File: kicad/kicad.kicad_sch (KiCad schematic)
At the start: 28 parts, among them J1 OLED_128x64, SW1 RotaryEncoder_Switch, SW2 SW_Wuerth_450301014042

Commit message: updated schematic and pcb
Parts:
- removed LED1: LED_5mm, PCM_LED_THT_AKL:LED_D5.0mm, symbol PCM_LED_AKL:LED_5mm
- added A1: Adafruit_Feather_V2, Module:Adafruit_Feather, symbol MCU_Module:Adafruit_Feather_Generic
- S1, S10, S11, S12, S2, S3, S4, S5, S6, S7, S8, S9: footprint (none) -> PCM_Switch_Keyboard_Hotswap_Kailh:SW_Hotswap_Kailh_MX_1.00u
- SW1: footprint (none) -> ScottoKeebs_Scotto:Encoder_EC11_MX
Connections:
- net +3V3: now also A1.2 (3V); no longer J1.2 (VCC)
- net COL0: now also A1.20 (13)
- net COL1: now also A1.21 (12)
- net COL2: now also A1.22 (27)
- net ENC_CLK: now also A1.5 (A0)
- net ENC_DT: now also A1.6 (A1)
- net ENC_SW: now also A1.7 (A2)
- net GND: now also SW2.2 (C), A1.4 (GND); no longer J1.1 (GND)
- net ROW0: now also A1.23 (33)
- net ROW1: now also A1.24 (15)
- net ROW2: now also A1.25 (32)
- net ROW3: now also A1.26 (14)
- net BT_SELECT: now reaches SW2.1 (B)
- net BT_SELECT: now also A1.8 (A3)
- net I2C_SCL: no longer names the net of J1.3 (SCL)
- net I2C_SDA: no longer names the net of J1.4 (SDA)
- no-connect marks 0 -> 5
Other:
- note added: "Connected with STEMMA QT directly to the board"

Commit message: modified layout to be 3 row 4 col instead of 3 col 4 row. added mounting holes
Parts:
- added H1, H2, H3, H4: MountingHole, MountingHole:MountingHole_2.2mm_M2, symbol Mechanical:MountingHole
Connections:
- net ROW3 is gone; now on net ROW2: A1.26 (14), D10.1 (K), D11.1 (K), D12.1 (K)
- net BT_SELECT: now also A1.6 (A1); no longer A1.8 (A3)
- net COL0: now also S5.1, S9.1; no longer S10.1, S4.1, S7.1
- net COL1: now also S10.1, S6.1; no longer S11.1, S5.1, S8.1
- net COL2: now also S11.1, S7.1; no longer S12.1, S6.1, S9.1
- net ENC_CLK: now also A1.8 (A3); no longer A1.5 (A0)
- net ENC_DT: now also A1.5 (A0); no longer A1.6 (A1)
- net ENC_SW: now also SW1.S2; no longer SW1.S1
- net GND: now also SW1.S1; no longer SW1.S2
- net ROW0: now also A1.24 (15), D4.1 (K); no longer A1.23 (33)
- net ROW1: now also A1.25 (32), D7.1 (K), D8.1 (K); no longer A1.24 (15), D4.1 (K)
- net ROW2: no longer A1.25 (32), D7.1 (K), D8.1 (K)
- new net COL3: A1.23 (33), S12.1, S4.1, S8.1
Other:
- moved on the sheet: A1, J1, SW1, SW2

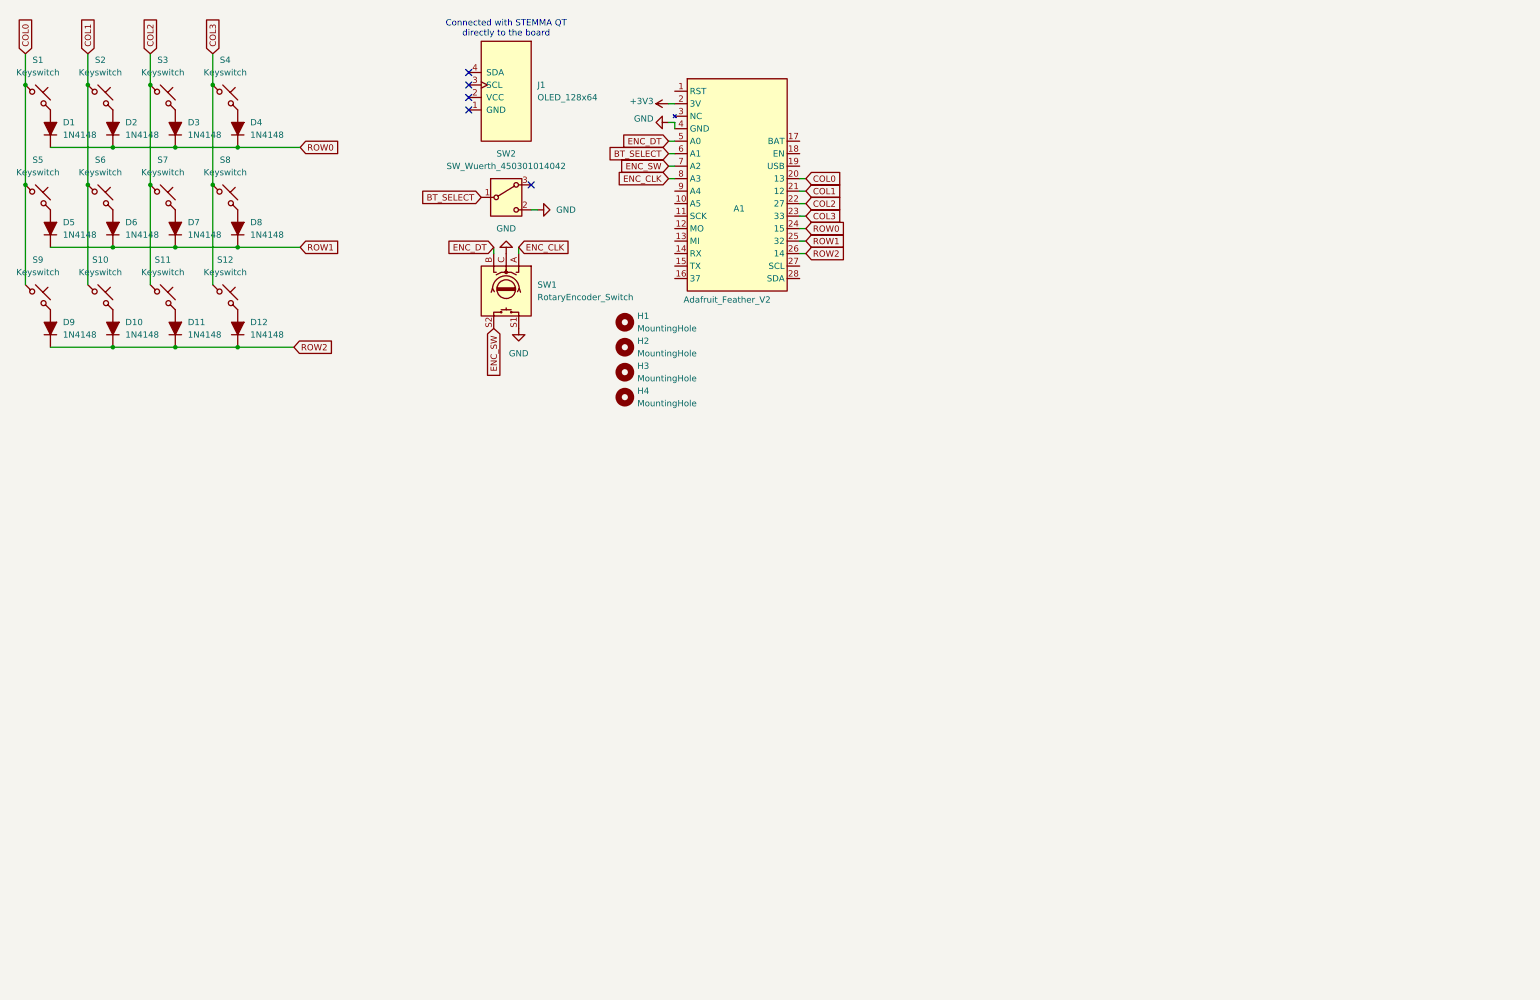
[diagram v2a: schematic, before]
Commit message: Updated schematic to change from single pcb to sandwich pcb.
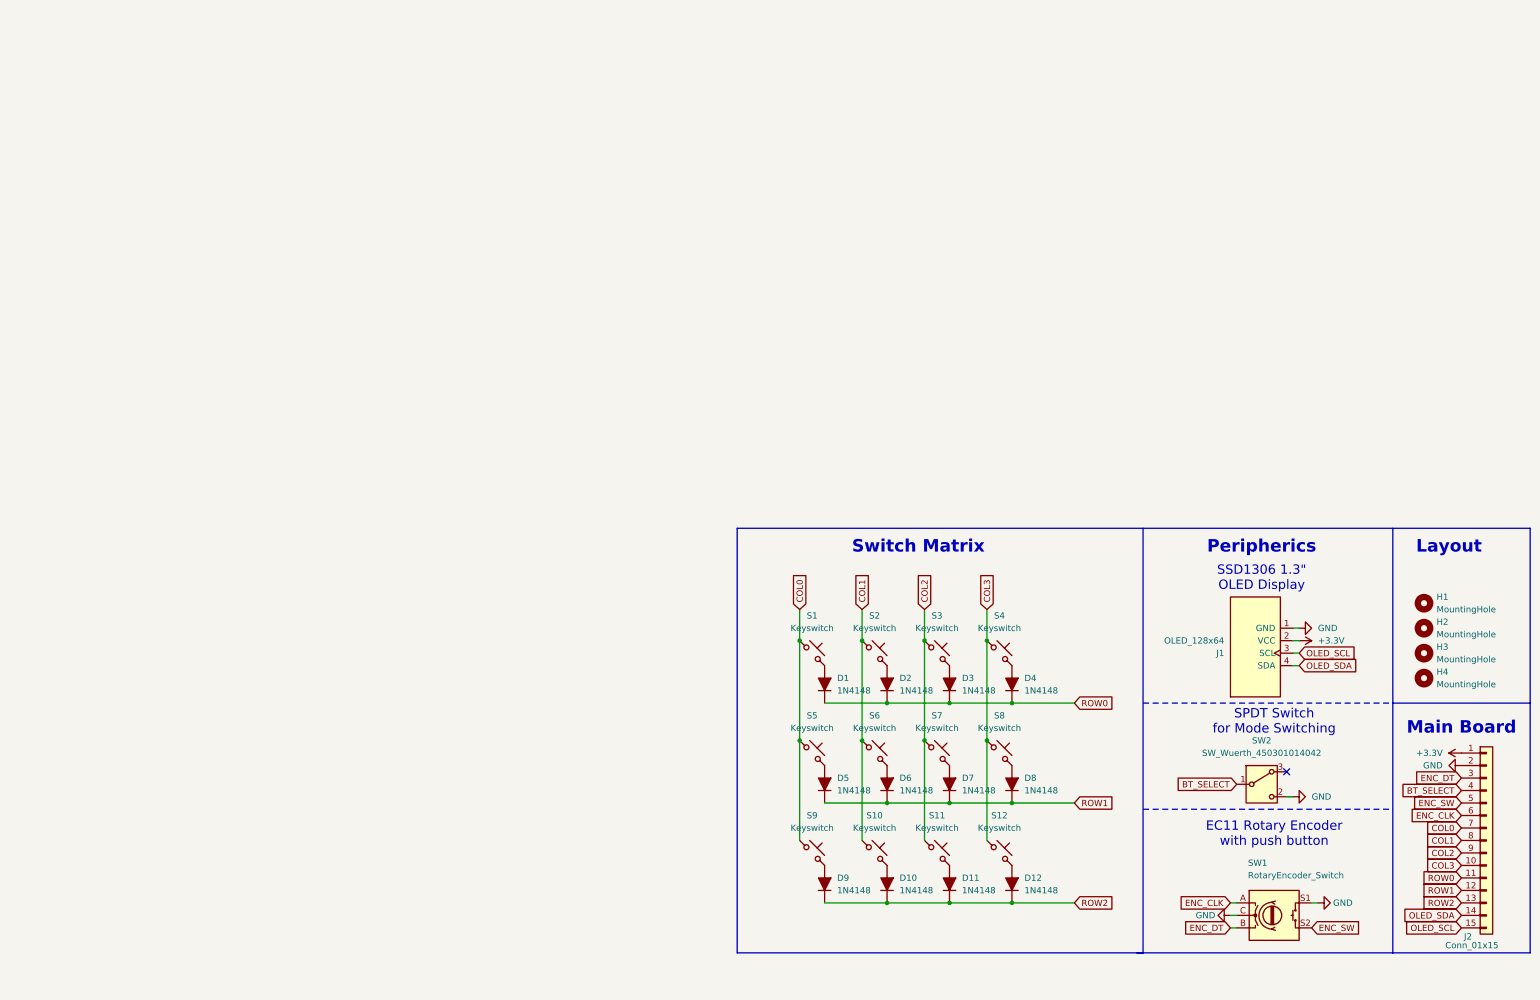
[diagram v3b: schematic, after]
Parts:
- removed A1: Adafruit_Feather_V2, Module:Adafruit_Feather, symbol MCU_Module:Adafruit_Feather_Generic
- added J2: Conn_01x15, symbol Connector_Generic:Conn_01x15
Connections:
- net BT_SELECT: now also J2.4 (Pin_4)
- net COL0: now also J2.7 (Pin_7)
- net COL1: now also J2.8 (Pin_8)
- net COL2: now also J2.9 (Pin_9)
- net COL3: now also J2.10 (Pin_10)
- net ENC_CLK: now also J2.6 (Pin_6)
- net ENC_DT: now also J2.3 (Pin_3)
- net ENC_SW: now also J2.5 (Pin_5)
- net GND: now also J1.1 (GND), J2.2 (Pin_2)
- net ROW0: now also J2.11 (Pin_11)
- net ROW1: now also J2.12 (Pin_12)
- net ROW2: now also J2.13 (Pin_13)
- net +3.3V: now reaches J1.2 (VCC)
- net +3.3V: now also J2.1 (Pin_1)
- net OLED_SCL: now reaches J1.3 (SCL)
- net OLED_SCL: now also J2.15 (Pin_15)
- net OLED_SDA: now reaches J1.4 (SDA)
- net OLED_SDA: now also J2.14 (Pin_14)
- no-connect marks 5 -> 1
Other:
- note added: "EC11 Rotary Encoder with push button"
- note added: "Layout"
- note added: "Main Board"
- note added: "Peripherics"
- note added: "SPDT Switch for Mode Switching"
- note added: "SSD1306 1.3" OLED Display"
- note added: "Switch Matrix"
- note removed: "Connected with STEMMA QT directly to the board"
- moved on the sheet: D1, D10, D11, D12, D2, D3, D4, D5, D6, D7, D8, D9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

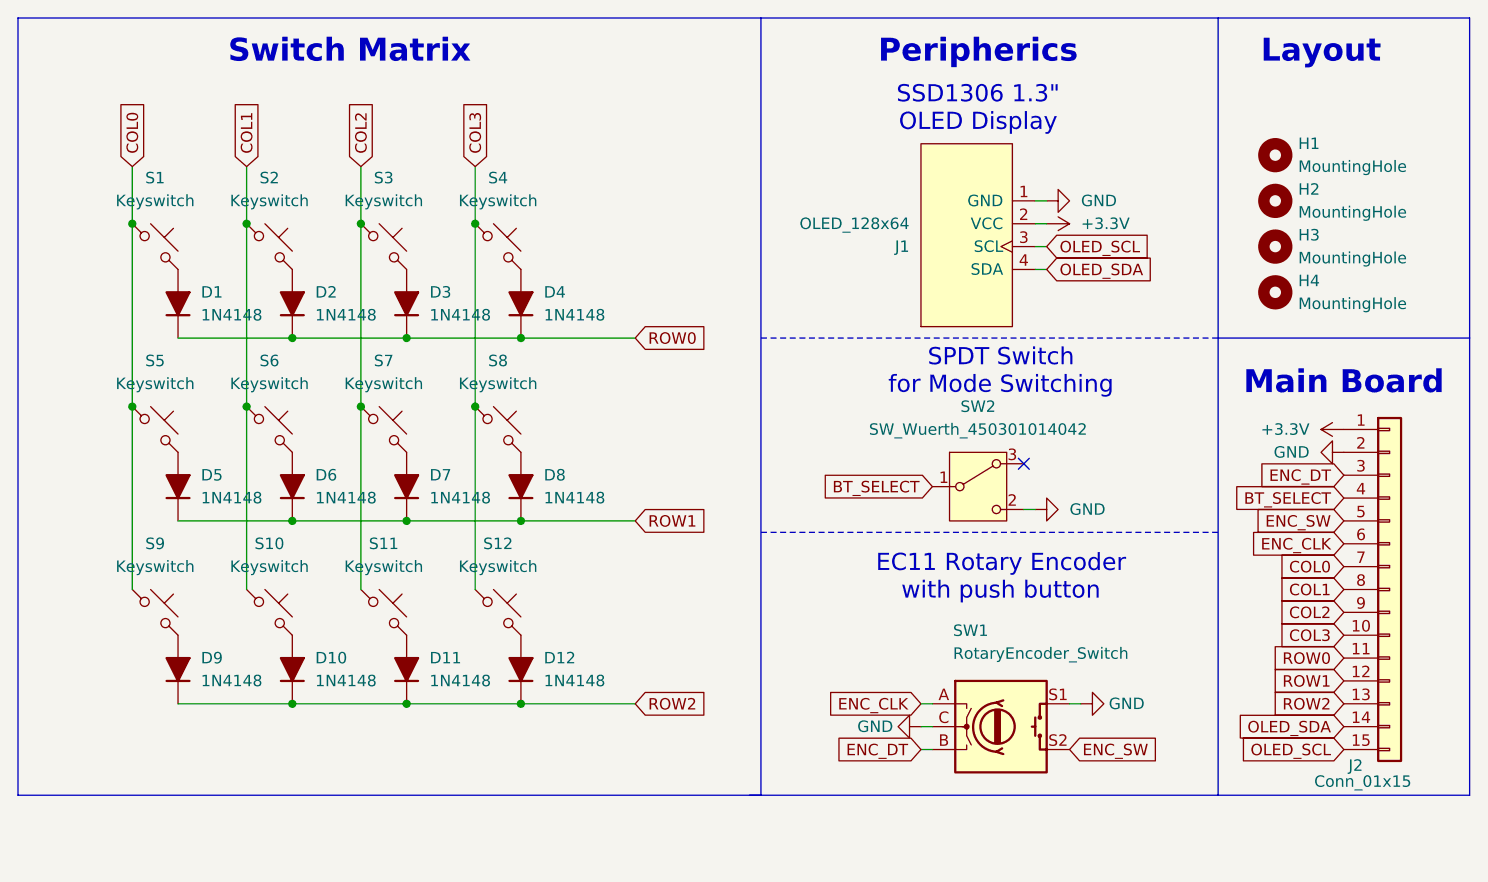
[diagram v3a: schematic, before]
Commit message: added 3d model for oled 128 x 64. went back to 3 x 4 format
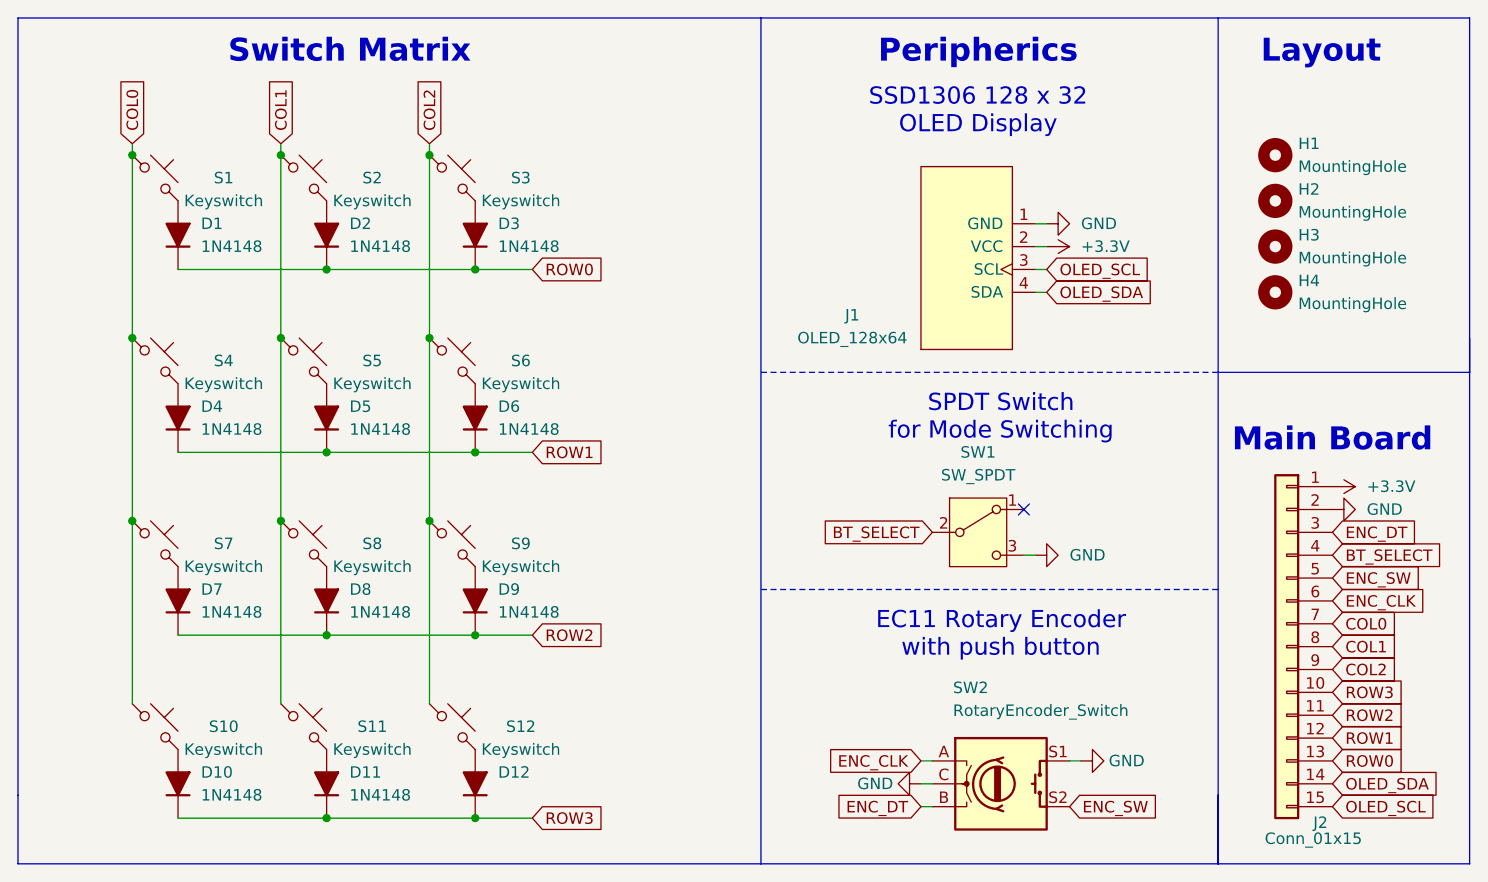
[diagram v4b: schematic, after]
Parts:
- removed D4, D8: 1N4148, PCM_Diode_THT_AKL:D_DO-35_SOD27_P7.62mm_Horizontal, symbol PCM_Diode_AKL:1N4148
- removed S4, S8: Keyswitch, PCM_Switch_Keyboard_Hotswap_Kailh:SW_Hotswap_Kailh_MX_1.00u, symbol ScottoKeebs:Placeholder_Keyswitch
- removed SW2: SW_Wuerth_450301014042, Button_Switch_THT:SW_Slide-03_Wuerth-WS-SLTV_10x2.5x6.4_P2.54mm, symbol Switch:SW_Wuerth_450301014042
- added D10, D11: 1N4148, Diode_THT:D_DO-35_SOD27_P7.62mm_Horizontal, symbol PCM_Diode_AKL:1N4148
- added S10, S11: Keyswitch, ScottoKeebs_Scotto:MX_Hotswap_1.00u, symbol ScottoKeebs:Placeholder_Keyswitch
- added SW1: SW_SPDT, Button_Switch_THT:SW_Slide_SPDT_Angled_CK_OS102011MA1Q, symbol Switch:SW_SPDT
- D1, D12, D2, D3: footprint PCM_Diode_THT_AKL:D_DO-35_SOD27_P7.62mm_Horizontal -> Diode_THT:D_DO-35_SOD27_P7.62mm_Horizontal
- D4: renamed from D5; footprint PCM_Diode_THT_AKL:D_DO-35_SOD27_P7.62mm_Horizontal -> Diode_THT:D_DO-35_SOD27_P7.62mm_Horizontal
- D5: renamed from D6; footprint PCM_Diode_THT_AKL:D_DO-35_SOD27_P7.62mm_Horizontal -> Diode_THT:D_DO-35_SOD27_P7.62mm_Horizontal
- D6: renamed from D7; footprint PCM_Diode_THT_AKL:D_DO-35_SOD27_P7.62mm_Horizontal -> Diode_THT:D_DO-35_SOD27_P7.62mm_Horizontal
- D7: renamed from D9; footprint PCM_Diode_THT_AKL:D_DO-35_SOD27_P7.62mm_Horizontal -> Diode_THT:D_DO-35_SOD27_P7.62mm_Horizontal
- D8: renamed from D10; footprint PCM_Diode_THT_AKL:D_DO-35_SOD27_P7.62mm_Horizontal -> Diode_THT:D_DO-35_SOD27_P7.62mm_Horizontal
- D9: renamed from D11; footprint PCM_Diode_THT_AKL:D_DO-35_SOD27_P7.62mm_Horizontal -> Diode_THT:D_DO-35_SOD27_P7.62mm_Horizontal
- J2: footprint (none) -> Connector_PinHeader_2.54mm:PinHeader_1x15_P2.54mm_Vertical
- S1, S12, S2, S3: footprint PCM_Switch_Keyboard_Hotswap_Kailh:SW_Hotswap_Kailh_MX_1.00u -> ScottoKeebs_Scotto:MX_Hotswap_1.00u
- S4: renamed from S5; footprint PCM_Switch_Keyboard_Hotswap_Kailh:SW_Hotswap_Kailh_MX_1.00u -> ScottoKeebs_Scotto:MX_Hotswap_1.00u
- S5: renamed from S6; footprint PCM_Switch_Keyboard_Hotswap_Kailh:SW_Hotswap_Kailh_MX_1.00u -> ScottoKeebs_Scotto:MX_Hotswap_1.00u
- S6: renamed from S7; footprint PCM_Switch_Keyboard_Hotswap_Kailh:SW_Hotswap_Kailh_MX_1.00u -> ScottoKeebs_Scotto:MX_Hotswap_1.00u
- S7: renamed from S9; footprint PCM_Switch_Keyboard_Hotswap_Kailh:SW_Hotswap_Kailh_MX_1.00u -> ScottoKeebs_Scotto:MX_Hotswap_1.00u
- S8: renamed from S10; footprint PCM_Switch_Keyboard_Hotswap_Kailh:SW_Hotswap_Kailh_MX_1.00u -> ScottoKeebs_Scotto:MX_Hotswap_1.00u
- S9: renamed from S11; footprint PCM_Switch_Keyboard_Hotswap_Kailh:SW_Hotswap_Kailh_MX_1.00u -> ScottoKeebs_Scotto:MX_Hotswap_1.00u
- renumbered SW1 to SW2
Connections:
- net BT_SELECT: now also SW1.2 (B)
- net COL0: now also S10.1
- net COL1: now also S11.1
- net COL2: now also S12.1
- net GND: now also SW1.3 (C)
- net ROW0: now also J2.13 (Pin_13); no longer J2.11 (Pin_11)
- net ROW2: now also J2.11 (Pin_11); no longer D12.1 (K), J2.13 (Pin_13)
- net COL3 renamed ROW3
- net ROW3: now also D12.1 (K), D10.1 (K), D11.1 (K); no longer S12.1
- new net: D11.2 (A), S11.2
- new net: D10.2 (A), S10.2
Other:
- note added: "SSD1306 128 x 32 OLED Display"
- note removed: "SSD1306 1.3" OLED Display"
- moved on the sheet: D1, D2, D3, D4, D5, D6, D7, D8, D9, J2, S1, S2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
